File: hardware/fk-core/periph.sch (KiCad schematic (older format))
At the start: 4 parts, among them M1 MICROSD, U5 PCF8523T

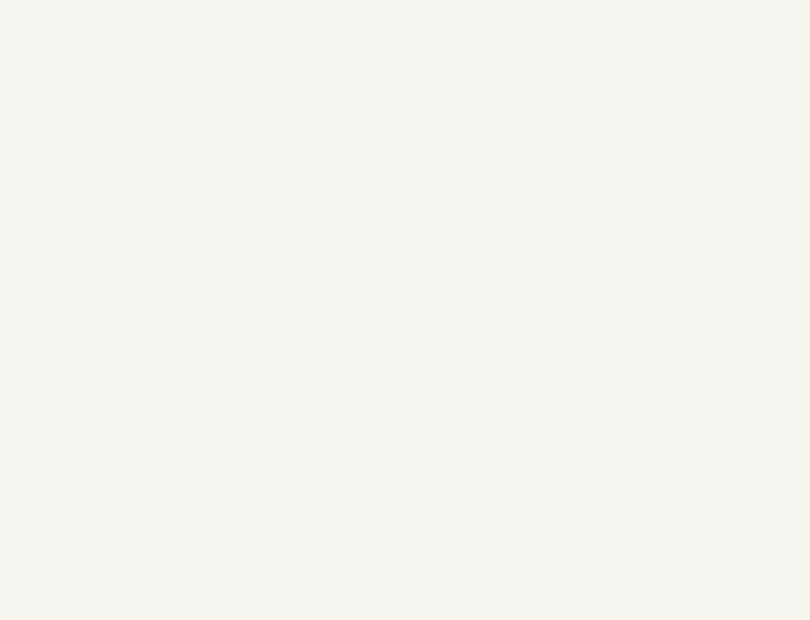
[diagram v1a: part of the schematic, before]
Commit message: Adding GPS connector and BOM placeholder.
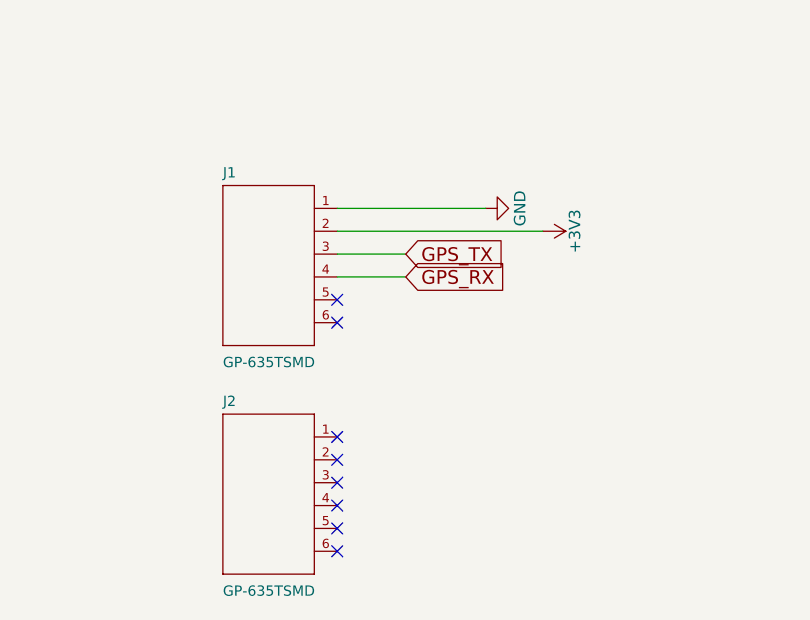
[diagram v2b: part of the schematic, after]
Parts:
- added J1: GP-635TSMD, SparkFun-Sensors_GP-635T, symbol GP-635TSMD
- added J2: GP-635TSMD, symbol GP-635TSMD
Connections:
- net +3V3: now also J1.2 (VCC)
- net GND: now also J1.1 (GND)
- new net GPS_RX: J1.4 (RXA)
- new net GPS_TX: J1.3 (TXA)
- no-connect marks 5 -> 13
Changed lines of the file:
@@
 LIBS:tps63060
 LIBS:max1704xx
+LIBS:gp-635tsmd
 LIBS:fk-core-cache
 EELAYER 25 0
@@
 $EndComp
 $Comp
-L +3V3 #PWR46
+L +3V3 #PWR052
 U 1 1 587FB329
 P 2050 2500
-F 0 "#PWR46" H 2050 2350 50  0001 C CNN
+F 0 "#PWR052" H 2050 2350 50  0001 C CNN
 F 1 "+3V3" H 2050 2640 50  0000 C CNN
 F 2 "" H 2050 2500 50  0000 C CNN
@@
 $EndComp
 $Comp
-L GND #PWR47
+L GND #PWR053
 U 1 1 587FB33D
 P 2050 3150
-F 0 "#PWR47" H 2050 2900 50  0001 C CNN
+F 0 "#PWR053" H 2050 2900 50  0001 C CNN
 F 1 "GND" H 2050 3000 50  0000 C CNN
 F 2 "" H 2050 3150 50  0000 C CNN
@@
 	4800 1850 4800 1950
 $Comp
-L +3V3 #PWR48
+L +3V3 #PWR054
 U 1 1 587FBC3F
 P 4800 1600
-F 0 "#PWR48" H 4800 1450 50  0001 C CNN
+F 0 "#PWR054" H 4800 1450 50  0001 C CNN
 F 1 "+3V3" H 4800 1740 50  0000 C CNN
 F 2 "" H 4800 1600 50  0000 C CNN
@@
 	4800 1750 6100 1750
 $Comp
-L GND #PWR49
+L GND #PWR055
 U 1 1 587FBD33
 P 4800 2550
-F 0 "#PWR49" H 4800 2300 50  0001 C CNN
+F 0 "#PWR055" H 4800 2300 50  0001 C CNN
 F 1 "GND" H 4800 2400 50  0000 C CNN
 F 2 "" H 4800 2550 50  0000 C CNN
@@
 NoConn ~ 7300 2350
 $Comp
-L PWR_FLAG #FLG7
+L PWR_FLAG #FLG056
 U 1 1 58811532
 P 4500 1850
-F 0 "#FLG7" H 4500 1945 50  0001 C CNN
+F 0 "#FLG056" H 4500 1945 50  0001 C CNN
 F 1 "PWR_FLAG" H 4500 2030 50  0000 C CNN
 F 2 "" H 4500 1850 50  0000 C CNN
@@
 Connection ~ 4800 1850
 NoConn ~ 1900 1500
+$Comp
+L GP-635TSMD J1
+U 1 1 58804955
+P 3350 4500
+F 0 "J1" H 3150 4830 45  0000 L BNN
+F 1 "GP-635TSMD" H 3150 4000 45  0000 L BNN
+F 2 "SparkFun-Sensors_GP-635T" H 3380 4650 20  0001 C CNN
+F 3 "" H 3350 4500 60  0001 C CNN
+F 4 "455-2875-1-ND" H 3350 4500 60  0001 C CNN "SPN"
+	1    3350 4500
+	1    0    0    -1
+$EndComp
+$Comp
+L GND #PWR057
+U 1 1 58804A10
+P 4300 4300
+F 0 "#PWR057" H 4300 4050 50  0001 C CNN
+F 1 "GND" H 4300 4150 50  0000 C CNN
+F 2 "" H 4300 4300 50  0000 C CNN
+F 3 "" H 4300 4300 50  0000 C CNN
+	1    4300 4300
+	0    -1   -1   0
+$EndComp
+Wire Wire Line
+	3650 4300 4300 4300
+$Comp
+L +3V3 #PWR058
+U 1 1 58804A47
+P 4550 4400
+F 0 "#PWR058" H 4550 4250 50  0001 C CNN
+F 1 "+3V3" H 4550 4540 50  0000 C CNN
+F 2 "" H 4550 4400 50  0000 C CNN
+F 3 "" H 4550 4400 50  0000 C CNN
+	1    4550 4400
+	0    1    1    0
+$EndComp
+Wire Wire Line
+	3650 4400 4550 4400
+Text GLabel 3950 4500 2    60   Input ~ 0
+GPS_TX
+Text GLabel 3950 4600 2    60   Input ~ 0
+GPS_RX
+Wire Wire Line
+	3650 4600 3950 4600
+Wire Wire Line
+	3950 4500 3650 4500
+NoConn ~ 3650 4700
+NoConn ~ 3650 4800
+$Comp
+L GP-635TSMD J2
+U 1 1 58805635
+P 3350 5500
+F 0 "J2" H 3150 5830 45  0000 L BNN
+F 1 "GP-635TSMD" H 3150 5000 45  0000 L BNN
+F 2 "" H 3380 5650 20  0001 C CNN
+F 3 "https://cdn.sparkfun.com/datasheets/GPS/GP-735T-150203.pdf" H 3350 5500 60  0001 C CNN
+F 4 "39.95" H 3350 5500 60  0001 C CNN "COST"
+	1    3350 5500
+	1    0    0    -1
+$EndComp
+NoConn ~ 3650 5800
+NoConn ~ 3650 5700
+NoConn ~ 3650 5600
+NoConn ~ 3650 5500
+NoConn ~ 3650 5400
+NoConn ~ 3650 5300
 $EndSCHEMATC

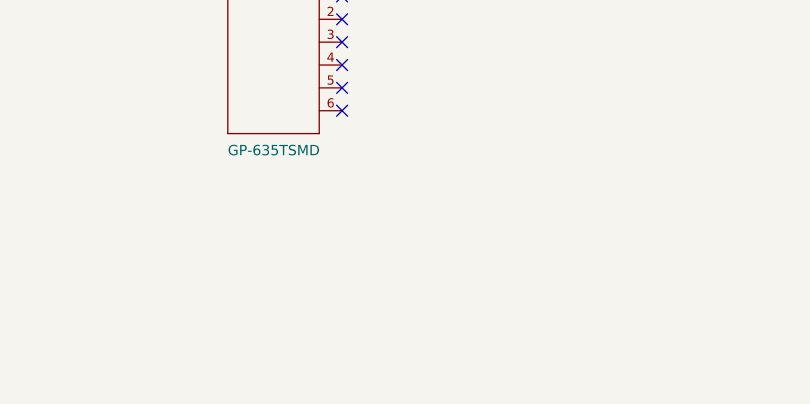
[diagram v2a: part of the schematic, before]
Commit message: Assigning most of the footprints.
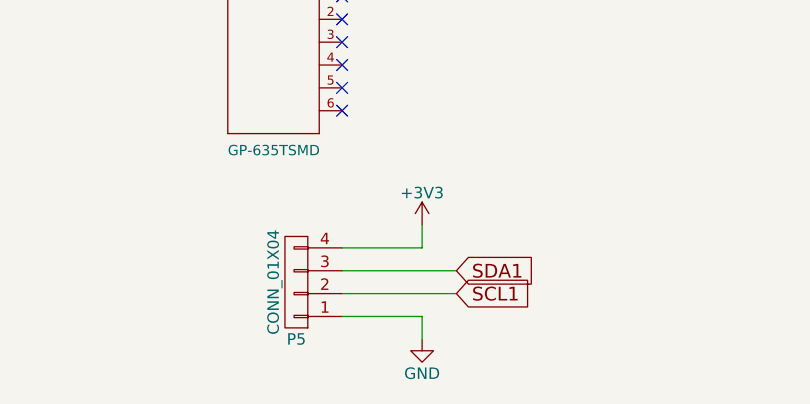
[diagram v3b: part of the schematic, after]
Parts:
- added P5: CONN_01X04, Socket_Strips:Socket_Strip_Straight_1x04, symbol CONN_01X04
- BT1: footprint (none) -> Connectors:CR1220
- CRYSTAL8X3.8SMT1: footprint (none) -> SOJ-4:SOJ-4
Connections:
- net +3V3: now also P5.4 (P4)
- net GND: now also P5.1 (P1)
- net SCL1: now also P5.2 (P2)
- net SDA1: now also P5.3 (P3)
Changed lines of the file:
@@
 F 0 "BT1" H 4900 2250 50  0000 L CNN
 F 1 "Battery_Cell" H 4900 2150 50  0000 L CNN
-F 2 "" V 4800 2210 50  0000 C CNN
+F 2 "Connectors:CR1220" V 4800 2210 50  0001 C CNN
 F 3 "" V 4800 2210 50  0000 C CNN
 F 4 "BC501SM-ND" H 4800 2150 60  0001 C CNN "SPN"
@@
 F 0 "CRYSTAL8X3.8SMT1" H 7750 2100 50  0000 C CNN
 F 1 "Crystal" H 7750 1800 50  0000 C CNN
-F 2 "" H 7750 1950 50  0000 C CNN
+F 2 "SOJ-4:SOJ-4" H 7750 1950 50  0001 C CNN
 F 3 "" H 7750 1950 50  0000 C CNN
 F 4 "XC1912CT-ND" H 7750 1950 60  0001 C CNN "SPN"
@@
 NoConn ~ 3650 5400
 NoConn ~ 3650 5300
+$Comp
+L CONN_01X04 P5
+U 1 1 58806947
+P 3450 6550
+F 0 "P5" H 3450 6800 50  0000 C CNN
+F 1 "CONN_01X04" V 3550 6550 50  0000 C CNN
+F 2 "Socket_Strips:Socket_Strip_Straight_1x04" H 3450 6550 50  0001 C CNN
+F 3 "" H 3450 6550 50  0000 C CNN
+	1    3450 6550
+	-1   0    0    1
+$EndComp
+Text GLabel 4150 6500 2    60   Input ~ 0
+SDA1
+Text GLabel 4150 6600 2    60   Input ~ 0
+SCL1
+$Comp
+L +3V3 #PWR059
+U 1 1 58806AD4
+P 4000 6300
+F 0 "#PWR059" H 4000 6150 50  0001 C CNN
+F 1 "+3V3" H 4000 6440 50  0000 C CNN
+F 2 "" H 4000 6300 50  0000 C CNN
+F 3 "" H 4000 6300 50  0000 C CNN
+	1    4000 6300
+	1    0    0    -1
+$EndComp
+Wire Wire Line
+	4000 6300 4000 6400
+Wire Wire Line
+	4000 6400 3650 6400
+$Comp
+L GND #PWR060
+U 1 1 58806B22
+P 4000 6800
+F 0 "#PWR060" H 4000 6550 50  0001 C CNN
+F 1 "GND" H 4000 6650 50  0000 C CNN
+F 2 "" H 4000 6800 50  0000 C CNN
+F 3 "" H 4000 6800 50  0000 C CNN
+	1    4000 6800
+	1    0    0    -1
+$EndComp
+Wire Wire Line
+	4000 6800 4000 6700
+Wire Wire Line
+	4000 6700 3650 6700
+Wire Wire Line
+	4150 6600 3650 6600
+Wire Wire Line
+	3650 6500 4150 6500
 $EndSCHEMATC

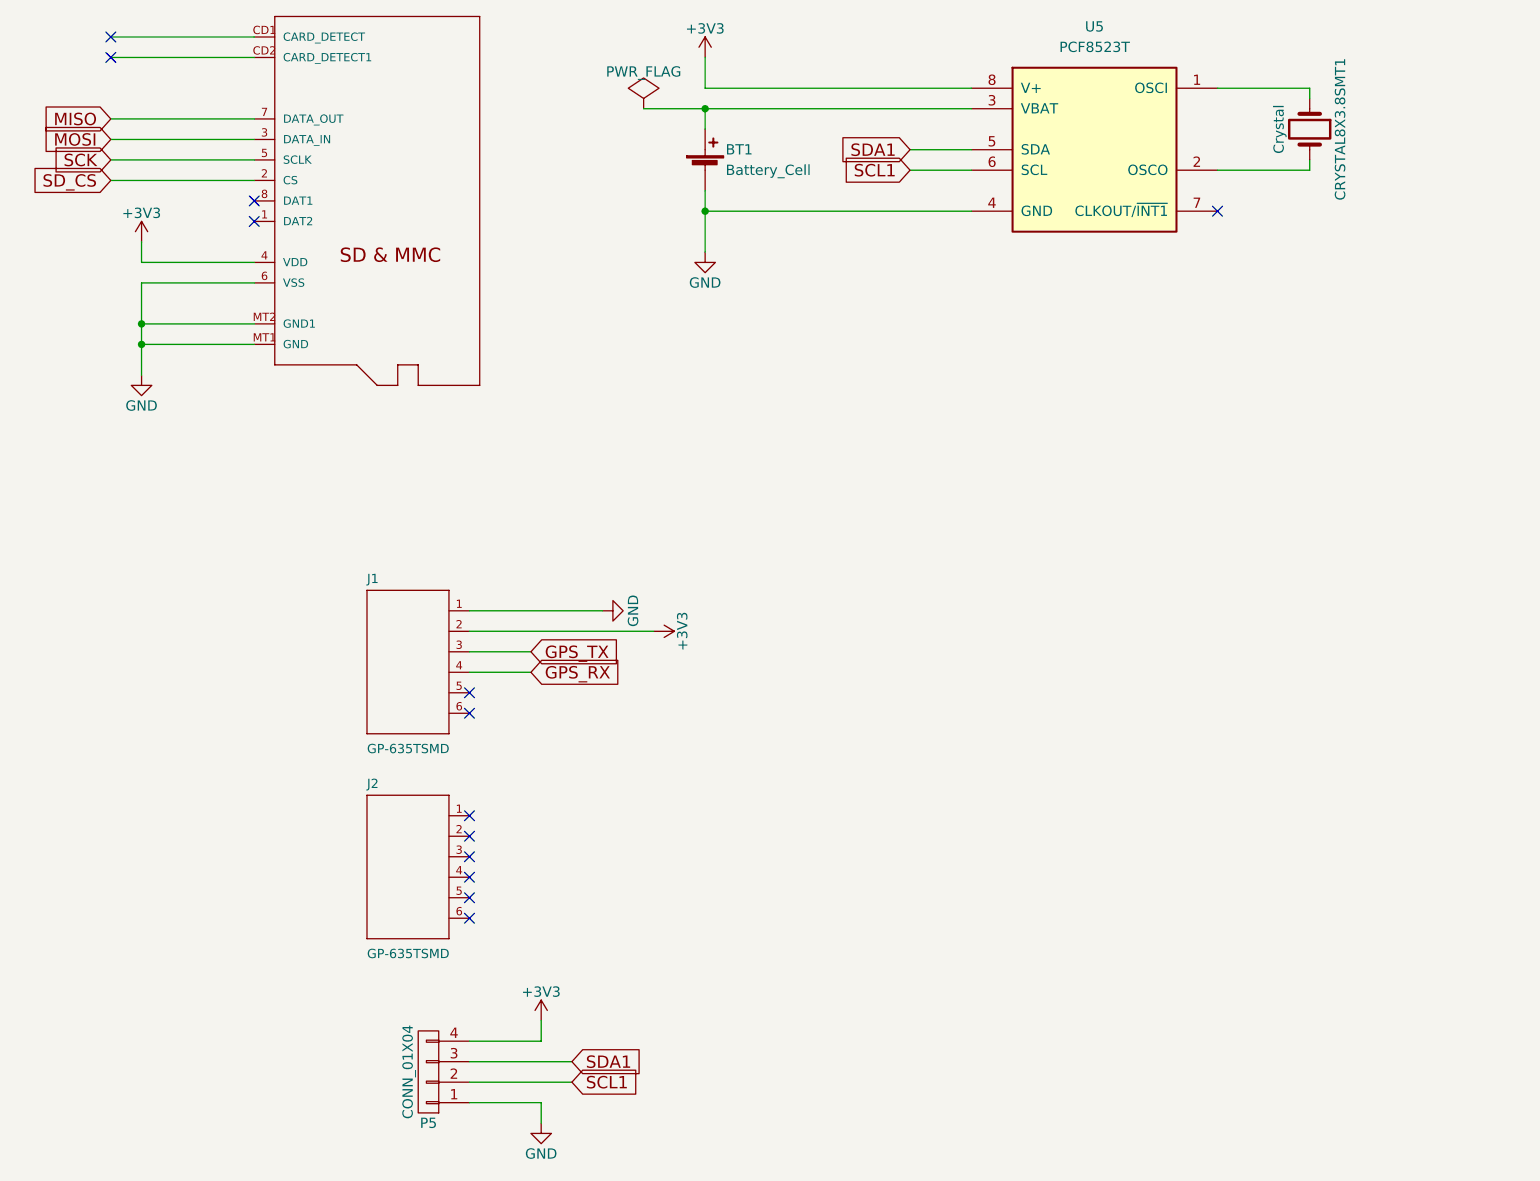
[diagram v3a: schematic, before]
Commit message: Better footprints, swapping GPS for FGPMMOPA6H
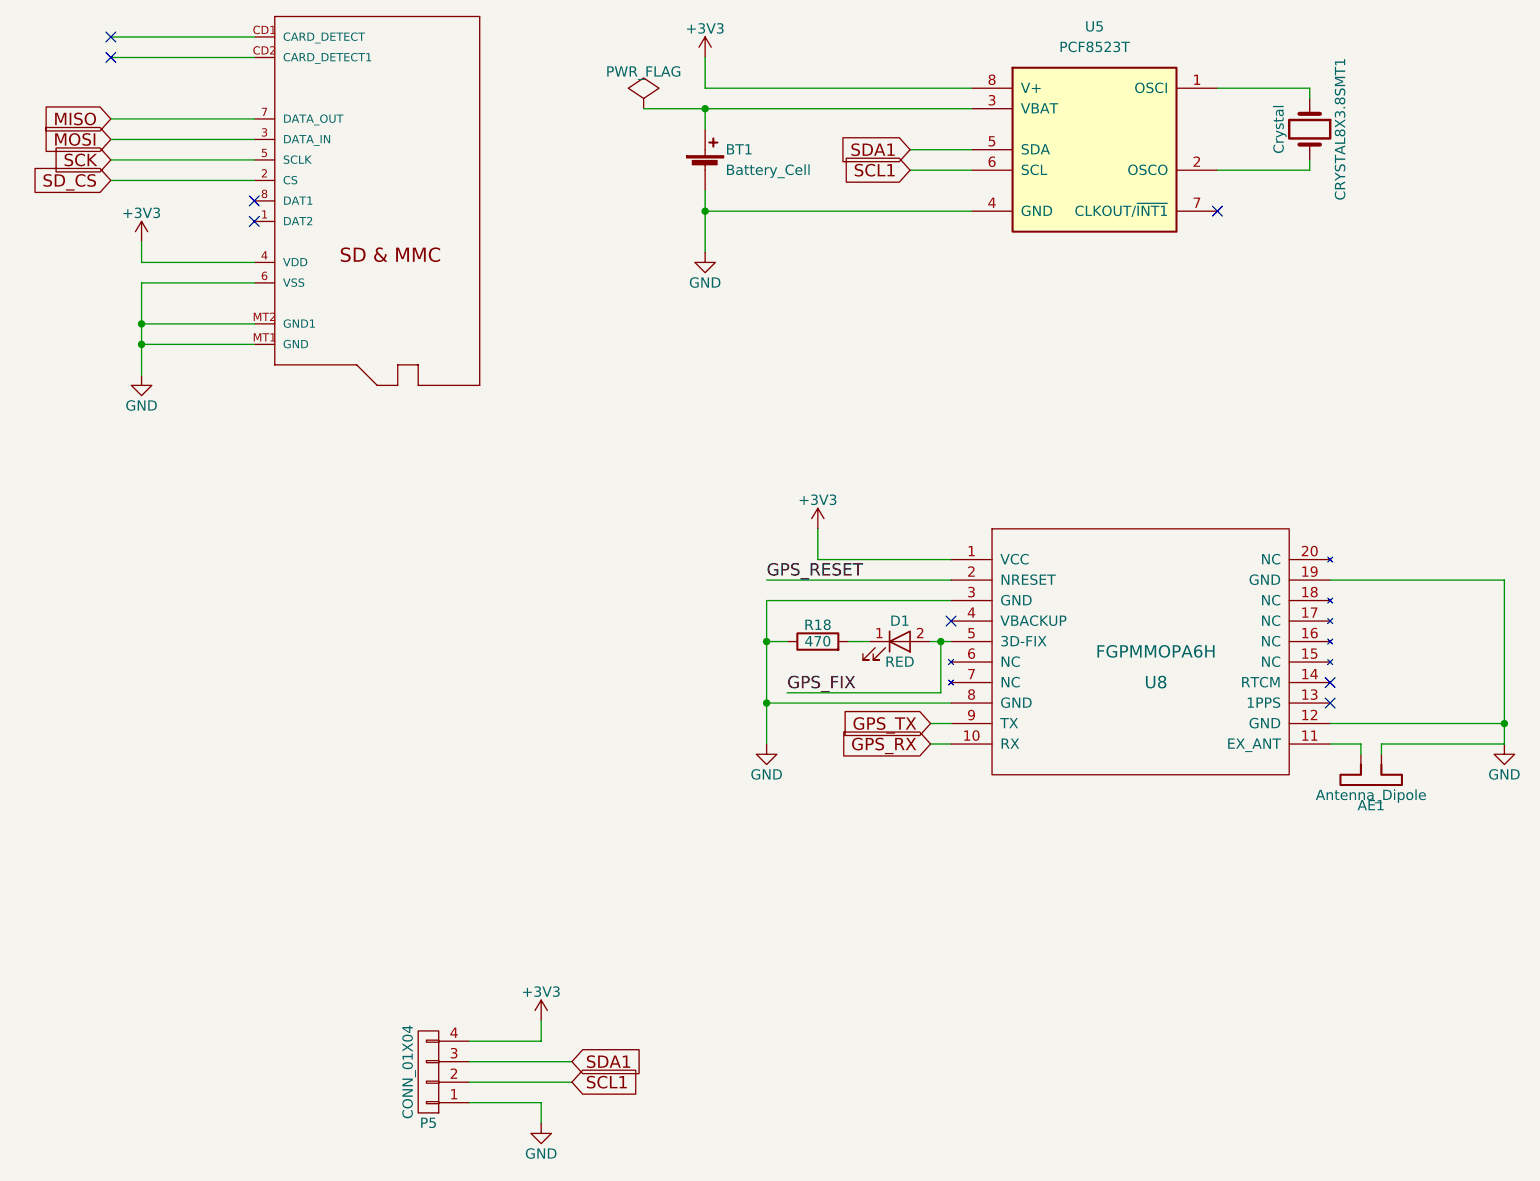
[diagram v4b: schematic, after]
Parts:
- removed J1: GP-635TSMD, SparkFun-Sensors_GP-635T, symbol GP-635TSMD
- removed J2: GP-635TSMD, symbol GP-635TSMD
- added AE1: Antenna_Dipole, symbol Antenna_Dipole
- added D1: RED, LEDs:LED_0805, symbol LED
- added R18: 470, Capacitors_SMD:C_0805_HandSoldering, symbol R
- added U8: FGPMMOPA6H, FGPMMOPA6H:FGPMMOPA6H, symbol FGPMMOPA6H
- M1: footprint adafruit_MICROSD -> microsd:MicroSD-Yamaichi-PJS
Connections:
- net +3V3: now also U8.1 (VCC)
- net GND: now also AE1.1, R18.1, U8.12 (GND), U8.19 (GND), U8.3 (GND), U8.8 (GND)
- net GPS_RX: now also U8.10 (RX)
- net GPS_TX: now also U8.9 (TX)
- new net: AE1.2, U8.11 (EX_ANT)
- new net: D1.1 (K), R18.2
- new net GPS_FIX: D1.2 (A), U8.5 (3D-FIX)
- new net GPS_RESET: U8.2 (NRESET)
- no-connect marks 13 -> 8
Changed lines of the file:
@@
 LIBS:max1704xx
 LIBS:gp-635tsmd
+LIBS:fgpmmopa6h
 LIBS:fk-core-cache
 EELAYER 25 0
@@
 F 0 "M1" H 3300 2200 45  0001 C CNN
 F 1 "MICROSD" H 3300 2200 45  0001 C CNN
-F 2 "adafruit_MICROSD" H 3330 2350 20  0001 C CNN
+F 2 "microsd:MicroSD-Yamaichi-PJS" H 3330 2350 20  0001 C CNN
 F 3 "" H 3300 2200 60  0001 C CNN
 F 4 "101-00581-59-1-ND" H 3300 2200 60  0001 C CNN "SPN"
@@
 Connection ~ 4800 1850
 NoConn ~ 1900 1500
-$Comp
-L GP-635TSMD J1
-U 1 1 58804955
-P 3350 4500
-F 0 "J1" H 3150 4830 45  0000 L BNN
-F 1 "GP-635TSMD" H 3150 4000 45  0000 L BNN
-F 2 "SparkFun-Sensors_GP-635T" H 3380 4650 20  0001 C CNN
-F 3 "" H 3350 4500 60  0001 C CNN
-F 4 "455-2875-1-ND" H 3350 4500 60  0001 C CNN "SPN"
-	1    3350 4500
-	1    0    0    -1
-$EndComp
-$Comp
-L GND #PWR057
-U 1 1 58804A10
-P 4300 4300
-F 0 "#PWR057" H 4300 4050 50  0001 C CNN
-F 1 "GND" H 4300 4150 50  0000 C CNN
-F 2 "" H 4300 4300 50  0000 C CNN
-F 3 "" H 4300 4300 50  0000 C CNN
-	1    4300 4300
-	0    -1   -1   0
-$EndComp
-Wire Wire Line
-	3650 4300 4300 4300
-$Comp
-L +3V3 #PWR058
-U 1 1 58804A47
-P 4550 4400
-F 0 "#PWR058" H 4550 4250 50  0001 C CNN
-F 1 "+3V3" H 4550 4540 50  0000 C CNN
-F 2 "" H 4550 4400 50  0000 C CNN
-F 3 "" H 4550 4400 50  0000 C CNN
-	1    4550 4400
-	0    1    1    0
-$EndComp
-Wire Wire Line
-	3650 4400 4550 4400
-Text GLabel 3950 4500 2    60   Input ~ 0
-GPS_TX
-Text GLabel 3950 4600 2    60   Input ~ 0
+Text GLabel 5900 4950 0    60   Input ~ 0
 GPS_RX
-Wire Wire Line
-	3650 4600 3950 4600
-Wire Wire Line
-	3950 4500 3650 4500
-NoConn ~ 3650 4700
-NoConn ~ 3650 4800
-$Comp
-L GP-635TSMD J2
-U 1 1 58805635
-P 3350 5500
-F 0 "J2" H 3150 5830 45  0000 L BNN
-F 1 "GP-635TSMD" H 3150 5000 45  0000 L BNN
-F 2 "" H 3380 5650 20  0001 C CNN
-F 3 "https://cdn.sparkfun.com/datasheets/GPS/GP-735T-150203.pdf" H 3350 5500 60  0001 C CNN
-F 4 "39.95" H 3350 5500 60  0001 C CNN "COST"
-	1    3350 5500
-	1    0    0    -1
-$EndComp
-NoConn ~ 3650 5800
-NoConn ~ 3650 5700
-NoConn ~ 3650 5600
-NoConn ~ 3650 5500
-NoConn ~ 3650 5400
-NoConn ~ 3650 5300
 $Comp
 L CONN_01X04 P5
@@
 SCL1
 $Comp
-L +3V3 #PWR059
+L +3V3 #PWR057
 U 1 1 58806AD4
 P 4000 6300
-F 0 "#PWR059" H 4000 6150 50  0001 C CNN
+F 0 "#PWR057" H 4000 6150 50  0001 C CNN
 F 1 "+3V3" H 4000 6440 50  0000 C CNN
 F 2 "" H 4000 6300 50  0000 C CNN
@@
 	4000 6400 3650 6400
 $Comp
-L GND #PWR060
+L GND #PWR058
 U 1 1 58806B22
 P 4000 6800
-F 0 "#PWR060" H 4000 6550 50  0001 C CNN
+F 0 "#PWR058" H 4000 6550 50  0001 C CNN
 F 1 "GND" H 4000 6650 50  0000 C CNN
 F 2 "" H 4000 6800 50  0000 C CNN
@@
 Wire Wire Line
 	3650 6500 4150 6500
+$Comp
+L FGPMMOPA6H U8
+U 1 1 5880828D
+P 7000 4500
+F 0 "U8" H 7000 4350 60  0000 C CNN
+F 1 "FGPMMOPA6H" H 7000 4500 60  0000 C CNN
+F 2 "FGPMMOPA6H:FGPMMOPA6H" H 7000 4500 60  0001 C CNN
+F 3 "https://cdn-shop.adafruit.com/datasheets/GlobalTop-FGPMMOPA6H-Datasheet-V0A.pdf" H 7000 4500 60  0001 C CNN
+F 4 "1530-1011-1-ND" H 7000 4500 60  0001 C CNN "SPN"
+	1    7000 4500
+	1    0    0    -1
+$EndComp
+$Comp
+L GND #PWR059
+U 1 1 5880889C
+P 5100 4950
+F 0 "#PWR059" H 5100 4700 50  0001 C CNN
+F 1 "GND" H 5100 4800 50  0000 C CNN
+F 2 "" H 5100 4950 50  0000 C CNN
+F 3 "" H 5100 4950 50  0000 C CNN
+	1    5100 4950
+	1    0    0    -1
+$EndComp
+Wire Wire Line
+	5100 4750 6000 4750
+Wire Wire Line
+	5100 4250 5100 4950
+Wire Wire Line
+	5100 4250 6000 4250
+Connection ~ 5100 4750
+NoConn ~ 6000 4350
+NoConn ~ 7850 4750
+NoConn ~ 7850 4650
+$Comp
+L GND #PWR060
+U 1 1 588089E8
+P 8700 4950
+F 0 "#PWR060" H 8700 4700 50  0001 C CNN
+F 1 "GND" H 8700 4800 50  0000 C CNN
+F 2 "" H 8700 4950 50  0000 C CNN
+F 3 "" H 8700 4950 50  0000 C CNN
+	1    8700 4950
+	1    0    0    -1
+$EndComp
+Wire Wire Line
+	8700 4150 8700 4950
+Wire Wire Line
+	7850 4850 8700 4850
+Wire Wire Line
+	7850 4150 8700 4150
+Connection ~ 8700 4850
+$Comp
+L +3V3 #PWR061
+U 1 1 58809394
+P 5350 3900
+F 0 "#PWR061" H 5350 3750 50  0001 C CNN
+F 1 "+3V3" H 5350 4040 50  0000 C CNN
+F 2 "" H 5350 3900 50  0000 C CNN
+F 3 "" H 5350 3900 50  0000 C CNN
+	1    5350 3900
+	1    0    0    -1
+$EndComp
+Wire Wire Line
+	6000 4050 5350 4050
+Wire Wire Line
+	5350 4050 5350 3900
+Text GLabel 5900 4850 0    60   Input ~ 0
+GPS_TX
+Wire Wire Line
+	6000 4950 5900 4950
+Wire Wire Line
+	5900 4850 6000 4850
+$Comp
+L R R18
+U 1 1 58809D8B
+P 5350 4450
+F 0 "R18" V 5430 4450 50  0000 C CNN
+F 1 "470" V 5350 4450 50  0000 C CNN
+F 2 "Capacitors_SMD:C_0805_HandSoldering" V 5280 4450 50  0001 C CNN
+F 3 "" H 5350 4450 50  0000 C CNN
+F 4 "541-470CCT-ND" H 5350 4450 60  0001 C CNN "SPN"
+	1    5350 4450
+	0    -1   -1   0
+$EndComp
+$Comp
+L LED D1
+U 1 1 58809DE8
+P 5750 4450
+F 0 "D1" H 5750 4550 50  0000 C CNN
+F 1 "RED" H 5750 4350 50  0000 C CNN
+F 2 "LEDs:LED_0805" H 5750 4450 50  0001 C CNN
+F 3 "" H 5750 4450 50  0000 C CNN
+F 4 "475-1415-1-ND" H 5750 4450 60  0001 C CNN "SPN"
+	1    5750 4450
+	1    0    0    -1
+$EndComp
+Wire Wire Line
+	6000 4450 5900 4450
+Wire Wire Line
+	5600 4450 5500 4450
+Wire Wire Line
+	5200 4450 5100 4450
+Connection ~ 5100 4450
+$Comp
+L Antenna_Dipole AE1
+U 1 1 5880A476
+P 8100 5200
+F 0 "AE1" H 8150 5250 50  0000 C CNN
+F 1 "Antenna_Dipole" H 8150 5200 50  0000 C CNN
+F 2 "" H 8100 5200 50  0001 C CNN
+F 3 "" H 8100 5200 50  0001 C CNN
+F 4 "H11891CT-ND" H 8100 5200 60  0001 C CNN "SPN"
+	1    8100 5200
+	-1   0    0    1
+$EndComp
+Wire Wire Line
+	8000 5000 8000 4950
+Wire Wire Line
+	8000 4950 7850 4950
+Wire Wire Line
+	8100 5000 8100 4950
+Wire Wire Line
+	8100 4950 8700 4950
+Wire Wire Line
+	6000 4150 5100 4150
+Wire Wire Line
+	5950 4450 5950 4700
+Wire Wire Line
+	5950 4700 5200 4700
+Connection ~ 5950 4450
+Text Label 5200 4700 0    60   ~ 0
+GPS_FIX
+Text Label 5100 4150 0    60   ~ 0
+GPS_RESET
 $EndSCHEMATC
